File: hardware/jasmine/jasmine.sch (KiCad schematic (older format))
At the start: 25 parts, among them J1 NEIGHBOR1, J2 NEIGHBOR2, J3 USB-MICRO-B-SHIELDED, J4 LIPO_BATT_CONN, J7 BONUS_ROW, P1 TEST_POINT, P2 TEST_POINT, P3 TEST_POINT, P4 TEST_POINT, P5 3.7_VDC, U1 MCP73831T

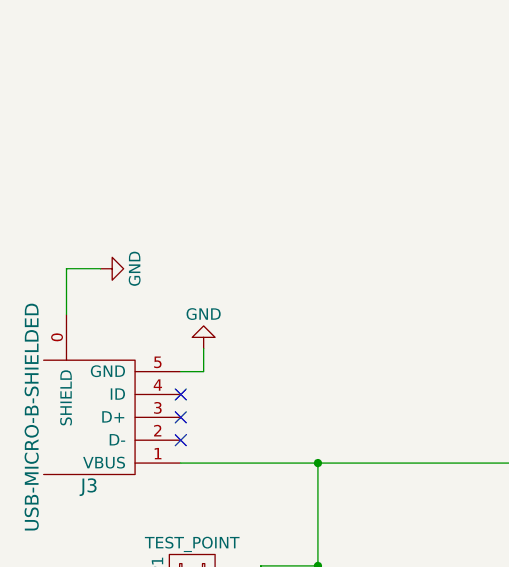
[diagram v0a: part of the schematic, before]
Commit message: Changed README.md and J3 no connect.
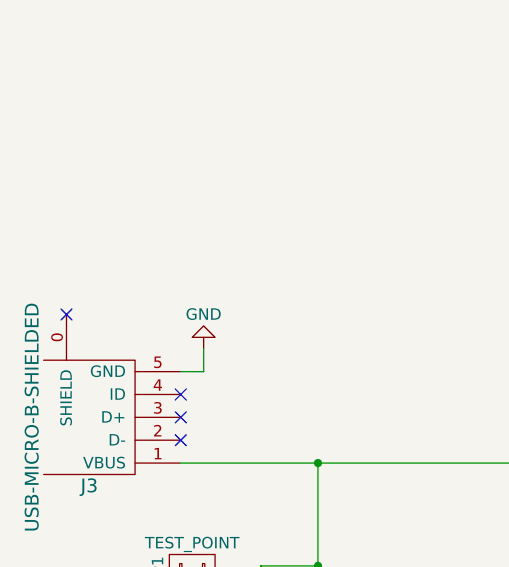
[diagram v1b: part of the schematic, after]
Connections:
- net GND: no longer J3.0 (SHIELD)
- no-connect marks 3 -> 4
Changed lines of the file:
@@
 Wire Wire Line
 	6150 7100 6150 6750
-$Comp
-L GND #PWR020
-U 1 1 5A0269D1
-P 4150 4200
-F 0 "#PWR020" H 4150 3950 50  0001 C CNN
-F 1 "GND" H 4150 4050 50  0000 C CNN
-F 2 "" H 4150 4200 50  0000 C CNN
-F 3 "" H 4150 4200 50  0000 C CNN
-	1    4150 4200
-	0    -1   -1   0
-$EndComp
-Wire Wire Line
-	4000 4400 4000 4200
-Wire Wire Line
-	4000 4200 4150 4200
+NoConn ~ 4000 4400
 $EndSCHEMATC

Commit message: Turned Jasmine into 2-layer board. Re-routes, fixes.
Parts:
- added R6: 0, gsg-modules:0603, symbol R
- added W1, W2: TEST, gsg-modules:0603-JUMPER, symbol TEST_2P
- U1: footprint gsg-modules:SOT-23-5 -> TO_SOT_Packages_SMD:SOT-23-5
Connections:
- net ADC0_0: now also W1.1
- net P4_3: now also W2.1; no longer R4.2, R5.1
- net P7_7: now also R6.2
- net VCC: no longer names the net of J1.2 (P2)
- net VCC: no longer J7.20 (P20)
- new net: R4.2, R5.1, R6.1, W1.2, W2.2
- no-connect marks 4 -> 96
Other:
- moved on the sheet: C1, C2, D1, D2, D3, J2, J3, J4, P1, P2, P3, P4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

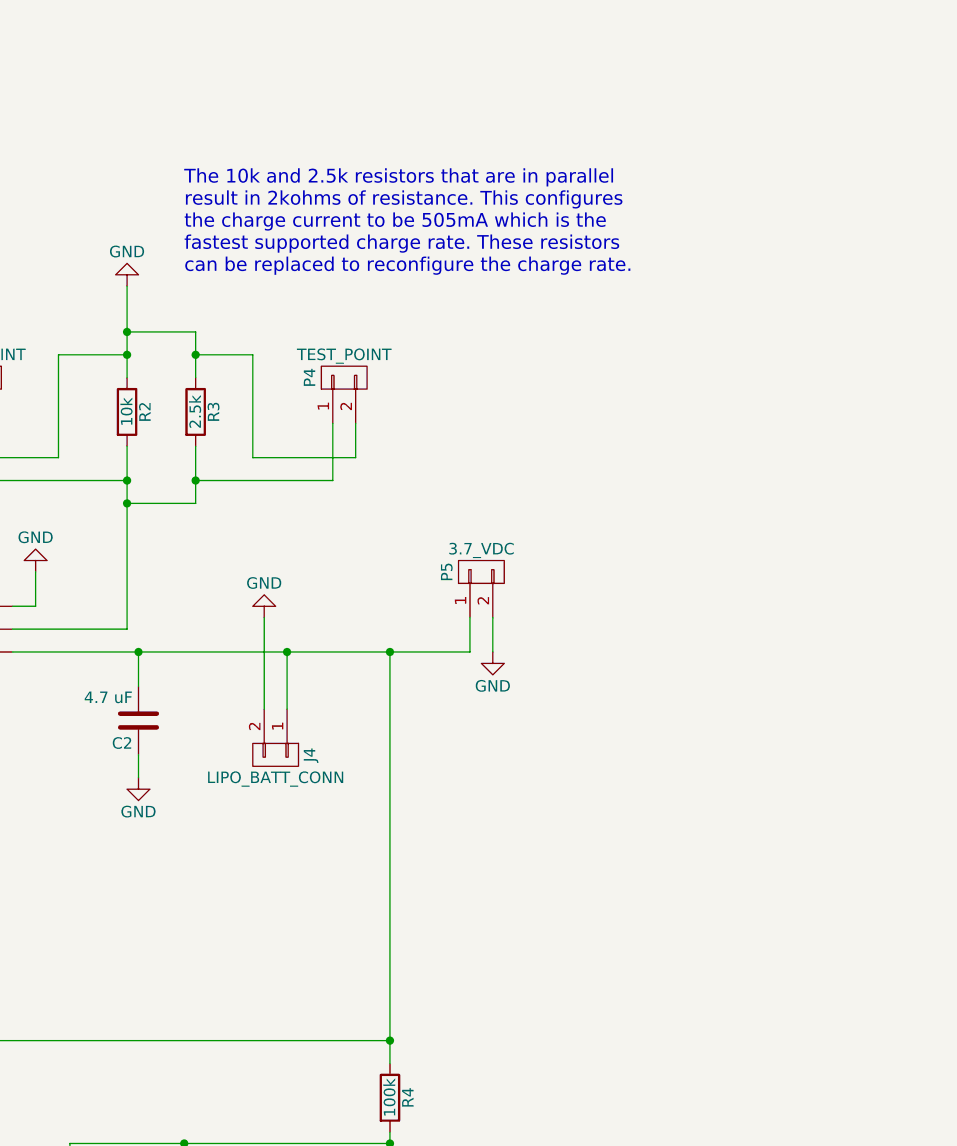
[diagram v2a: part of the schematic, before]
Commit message: Cleaning up GF and jasmine to fix local repo
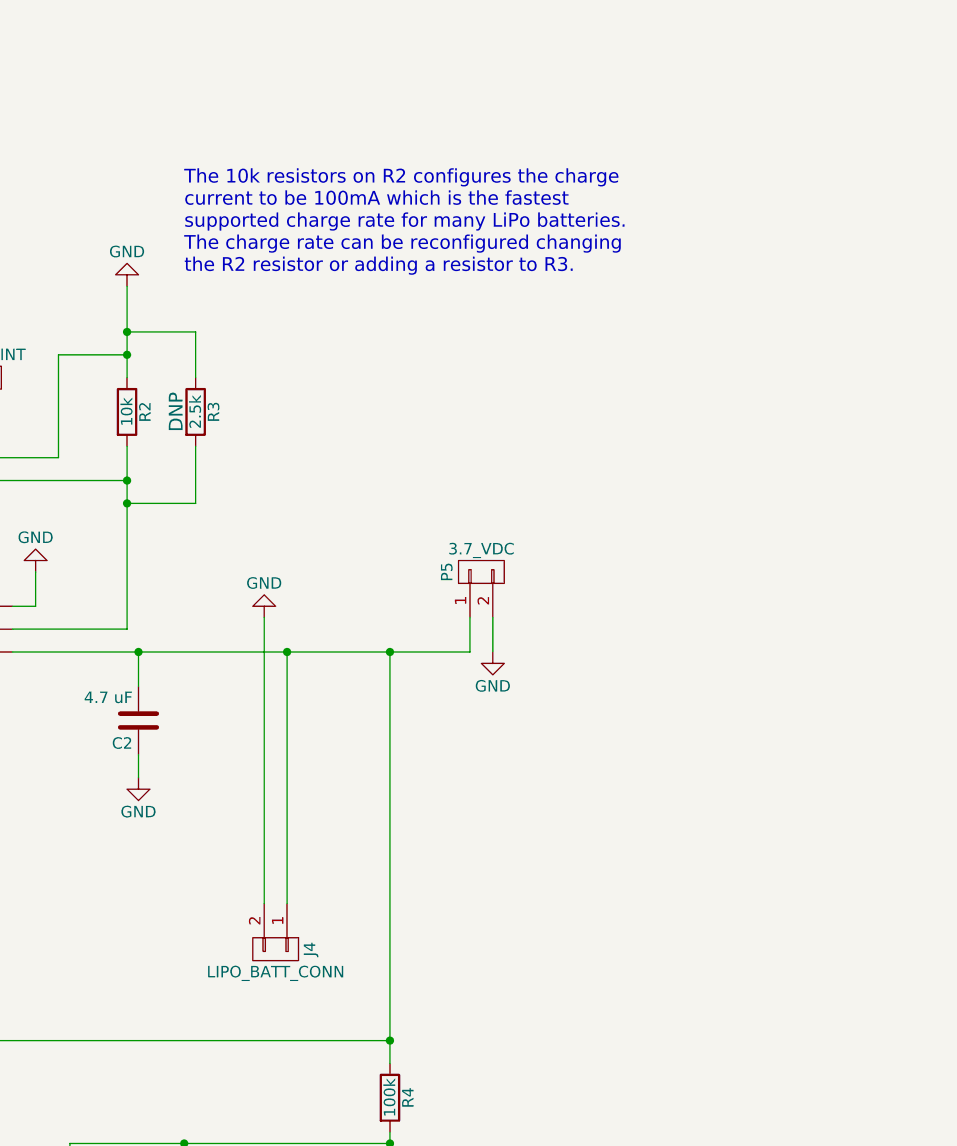
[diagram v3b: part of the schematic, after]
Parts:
- removed P4: TEST_POINT, gsg-modules:HEADER-1x2, symbol CONN_01X02
- R3: Note (none) -> DNP
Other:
- note added: "The 10k resistors on R2 configures the charge \ncurrent to be 100mA which is the fastest \nsupported charge rate for many LiPo batteries. \nThe charge rate can be reconfigured changing \nthe R2 resistor or adding a resistor to R3."
- note removed: "The 10k and 2.5k resistors that are in parallel \nresult in 2kohms of resistance. This configures \nthe charge current to be 505mA which is the \nfastest supported charge rate. These resistors \ncan be replaced to reconfigure the charge rate."
- moved on the sheet: J4
